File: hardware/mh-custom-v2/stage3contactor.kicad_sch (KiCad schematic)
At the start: 5 parts, among them J5 Screw_Terminal_01x04, J6 Screw_Terminal_01x04, J7 Screw_Terminal_01x04, J8 Screw_Terminal_01x04

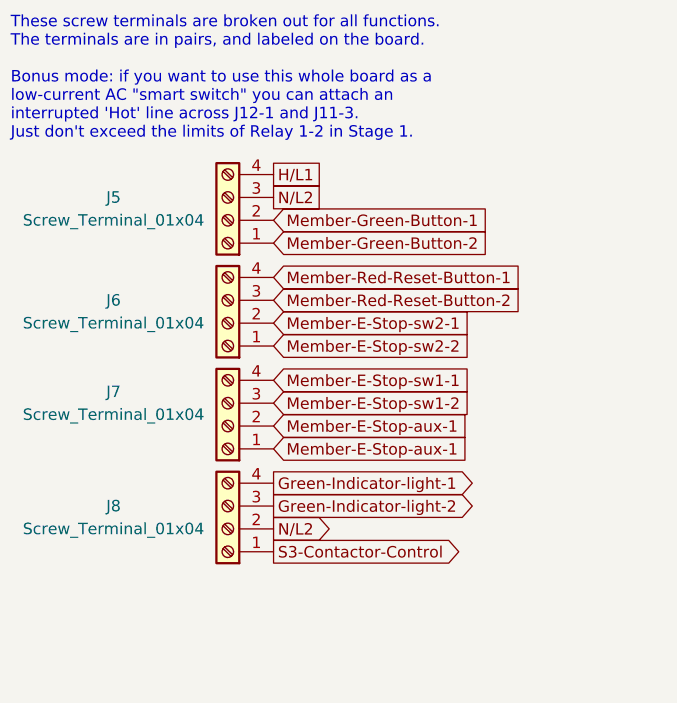
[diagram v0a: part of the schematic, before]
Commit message: low-voltage side of V2 board rebuilt. Started on high-voltage side
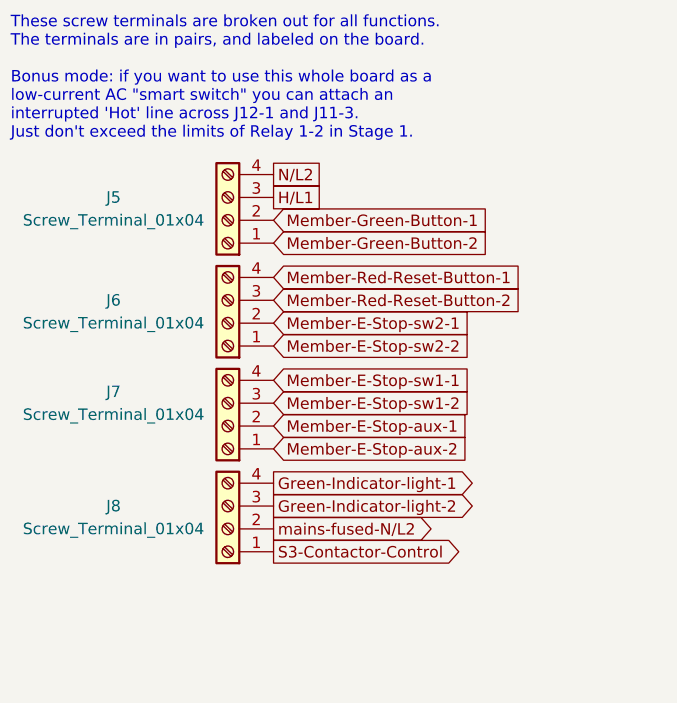
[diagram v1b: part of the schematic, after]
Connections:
- net H/L1: now also J5.3 (Pin_3); no longer J5.4 (Pin_4)
- net Member-E-Stop-aux-1: no longer J7.1 (Pin_1)
- net N/L2: now also J5.4 (Pin_4); no longer J5.3 (Pin_3), J8.2 (Pin_2)
- new net Member-E-Stop-aux-2: J7.1 (Pin_1)
- new net mains-fused-N/L2: J8.2 (Pin_2)
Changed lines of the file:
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@@
     )
   )
-  (global_label "H{slash}L1" (shape passive) (at 213.36 101.6 0) (fields_autoplaced)
+  (global_label "H{slash}L1" (shape passive) (at 213.36 104.14 0) (fields_autoplaced)
     (effects (font (size 1.27 1.27)) (justify left))
-    (property "Intersheet References" "${INTERSHEET_REFS}" (id 0) (at 220.6717 101.6794 0)
+    (property "Intersheet References" "${INTERSHEET_REFS}" (id 0) (at 220.6717 104.2194 0)
       (effects (font (size 1.27 1.27)) (justify left) hide)
     )
@@
     )
   )
-  (global_label "N{slash}L2" (shape output) (at 213.36 140.97 0) (fields_autoplaced)
+  (global_label "mains-fused-N{slash}L2" (shape output) (at 213.36 140.97 0) (fields_autoplaced)
     (effects (font (size 1.27 1.27)) (justify left))
-    (property "Intersheet References" "${INTERSHEET_REFS}" (id 0) (at 220.6717 140.8906 0)
+    (property "Intersheet References" "${INTERSHEET_REFS}" (id 0) (at 234.5812 140.8906 0)
       (effects (font (size 1.27 1.27)) (justify left) hide)
     )
@@
     )
   )
-  (global_label "Member-E-Stop-aux-1" (shape input) (at 213.36 132.08 0) (fields_autoplaced)
+  (global_label "Member-E-Stop-aux-2" (shape input) (at 213.36 132.08 0) (fields_autoplaced)
     (effects (font (size 1.27 1.27)) (justify left))
     (property "Intersheet References" "${INTERSHEET_REFS}" (id 0) (at 239.2379 132.0006 0)
@@
     )
   )
-  (global_label "N{slash}L2" (shape passive) (at 213.36 104.14 0) (fields_autoplaced)
+  (global_label "N{slash}L2" (shape passive) (at 213.36 101.6 0) (fields_autoplaced)
     (effects (font (size 1.27 1.27)) (justify left))
-    (property "Intersheet References" "${INTERSHEET_REFS}" (id 0) (at 220.6717 104.2194 0)
+    (property "Intersheet References" "${INTERSHEET_REFS}" (id 0) (at 220.6717 101.5206 0)
       (effects (font (size 1.27 1.27)) (justify left) hide)
     )

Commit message: approaching ordering from JLCPCB
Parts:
- F3: JLCPCB Part # (none) -> C206977
- J5, J6, J7, J8: JLCPCB Part # (none) -> C192769
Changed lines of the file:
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@@
+      (effects (font (size 1.27 1.27)) hide)
+    )
+    (property "JLCPCB Part #" "C192769" (id 4) (at 208.28 118.11 0)
       (effects (font (size 1.27 1.27)) hide)
     )
@@
       (effects (font (size 1.27 1.27)) hide)
     )
+    (property "JLCPCB Part #" "C206977" (id 4) (at 66.04 138.43 0)
+      (effects (font (size 1.27 1.27)) hide)
+    )
     (pin "1")
     (pin "2")
@@
     )
     (property "Datasheet" "~" (id 3) (at 208.28 140.97 0)
+      (effects (font (size 1.27 1.27)) hide)
+    )
+    (property "JLCPCB Part #" "C192769" (id 4) (at 208.28 140.97 0)
       (effects (font (size 1.27 1.27)) hide)
     )
@@
       (effects (font (size 1.27 1.27)) hide)
     )
+    (property "JLCPCB Part #" "C192769" (id 4) (at 208.28 106.68 0)
+      (effects (font (size 1.27 1.27)) hide)
+    )
     (pin "1")
     (pin "2")
@@
       (effects (font (size 1.27 1.27)) hide)
     )
+    (property "JLCPCB Part #" "C192769" (id 4) (at 208.28 129.54 0)
+      (effects (font (size 1.27 1.27)) hide)
+    )

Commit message: finalizing details of ordering from JLCPCB
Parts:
- F3: footprint Fuse:Fuseholder_Littelfuse_100_series_5x20mm -> Fuse:Fuseholder_Cylinder-5x20mm_Stelvio-Kontek_PTF78_Horizontal_Open; JLCPCB Part # C206977 -> C717030
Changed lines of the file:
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@@
       (effects (font (size 1.27 1.27)) (justify right))
     )
-    (property "Footprint" "Fuse:Fuseholder_Littelfuse_100_series_5x20mm" (id 2) (at 67.818 138.43 90)
+    (property "Footprint" "Fuse:Fuseholder_Cylinder-5x20mm_Stelvio-Kontek_PTF78_Horizontal_Open" (id 2) (at 67.818 138.43 90)
       (effects (font (size 1.27 1.27)) hide)
     )
@@
       (effects (font (size 1.27 1.27)) hide)
     )
-    (property "JLCPCB Part #" "C206977" (id 4) (at 66.04 138.43 0)
+    (property "JLCPCB Part #" "C717030" (id 4) (at 66.04 138.43 0)
       (effects (font (size 1.27 1.27)) hide)
     )

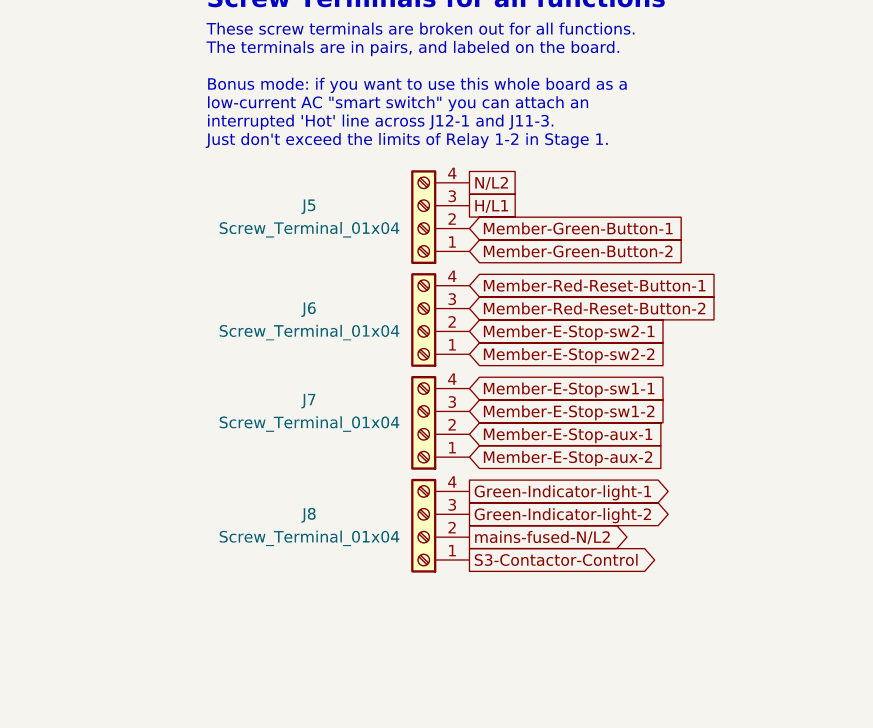
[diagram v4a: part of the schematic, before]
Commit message: improved some of the connections for easier soldering/production
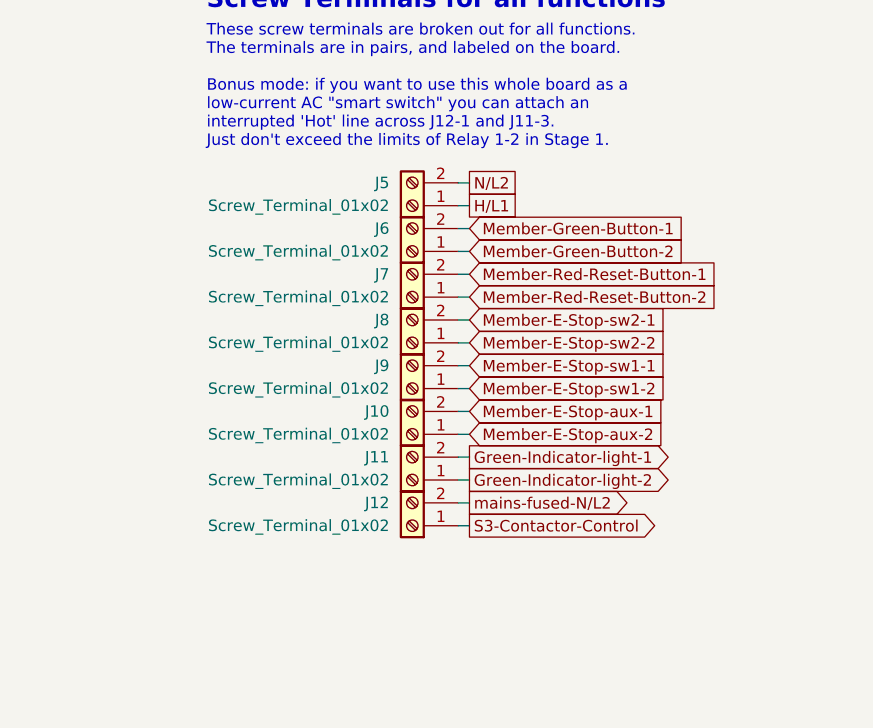
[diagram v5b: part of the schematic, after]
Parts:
- removed J5, J6, J7, J8: Screw_Terminal_01x04, TerminalBlock:TerminalBlock_Altech_AK300-4_P5.00mm, symbol Connector:Screw_Terminal_01x04
- added J10, J11, J12, J5, J6, J7, J8, J9: Screw_Terminal_01x02, TerminalBlock:TerminalBlock_Altech_AK300-2_P5.00mm, symbol Connector:Screw_Terminal_01x02
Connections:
- net Green-Indicator-light-1: now also J11.2 (Pin_2)
- net Green-Indicator-light-2: now also J11.1 (Pin_1)
- net H/L1: now also J5.1 (Pin_1)
- net Member-E-Stop-aux-1: now also J10.2 (Pin_2)
- net Member-E-Stop-aux-2: now also J10.1 (Pin_1)
- net Member-E-Stop-sw1-1: now also J9.2 (Pin_2)
- net Member-E-Stop-sw1-2: now also J9.1 (Pin_1)
- net Member-E-Stop-sw2-1: now also J8.2 (Pin_2)
- net Member-E-Stop-sw2-2: now also J8.1 (Pin_1)
- net Member-Green-Button-1: now also J6.2 (Pin_2)
- net Member-Green-Button-2: now also J6.1 (Pin_1)
- net Member-Red-Reset-Button-1: now also J7.2 (Pin_2)
- net Member-Red-Reset-Button-2: now also J7.1 (Pin_1)
- net N/L2: now also J5.2 (Pin_2)
- net S3-Contactor-Control: now also J12.1 (Pin_1)
- net mains-fused-N/L2: now also J12.2 (Pin_2)
